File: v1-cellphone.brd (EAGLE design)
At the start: 96 x 45.2 mm, 95 parts, among them J1 AVRISP, J2 ZX62D-B-5P8, J3 GPIO, J4 FTDI, J5 BATTERY INPUT, Q1 MIC, Q2 NTR4501N-D, Q3 NTR4501N-D, U1 MCP73831, U2 MEGA1284, U3 GSM_UC15, U4 TXB0104PWR, X1 SMA, X2 8MHz, X3 CCM03-3002 R102

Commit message: All tracks routed. Needs review and impedance checks.
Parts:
- removed J3: GPIO, SparkFun-Connectors:1X20_LOCK_LONGPADS
- removed TP17, TP2, TP4, TP5: TPPAD1-13, testpad:P1-13
- added JP1, JP2, JP3: (no value), SparkFun-Connectors:1X04_LOCK
- C22, C26: device rcl_custom:0603-B -> rcl_custom:C1210K
- moved SP1 571.4 mm to (96.0, 13.8), turned to 270 degrees
- moved C40 561.8 mm to (31.6, 40.6), turned to 90 degrees
- moved C2 544.5 mm to (39.2, 11.7)
- moved C41 543.2 mm to (44.3, 14.5)
- moved R13 541.2 mm to (45.0, 22.5), turned to 180 degrees
- moved R12 529.3 mm to (95.1, 3.17), turned to 270 degrees
- moved R11 529.2 mm to (97.4, 7.49), turned to 270 degrees
- moved Q3 519.8 mm to (92.3, 3.30), turned to 90 degrees
- moved U4 514.9 mm to (46.4, 18.5), turned to 90 degrees
- moved TP15 489.0 mm to (32.9, 24.0)
- moved TP14 483.4 mm to (34.5, 22.4)
- moved TP12 458.7 mm to (36.2, 24.0)
- moved TP11 453.2 mm to (37.8, 22.4)
- moved R14 451.0 mm to (62.6, 43.8), turned to 180 degrees
- moved TP13 448.1 mm to (4.95, 14.2)
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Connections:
- net N$10 renamed PRESENCE
- net N$14 renamed OE
- net N$16 renamed MIC1P
- net N$19 renamed MIC1N
- net N$7 renamed XTAL2
- net N$8 renamed XTAL1
- net PB4 renamed DEBUGLED
- removed net 2.6V: C39.1, R13.1, TP2.TP, U3.7, U4.1
- new net VDD_EXT: C39.1, R13.1, U3.7, U4.1
- net N$20: no longer TP4.TP
- net N$21: no longer TP5.TP
- net N$23: no longer TP17.TP
- net PA0: now also JP1.1; no longer J3.1
- net PA1: now also JP1.2; no longer J3.2
- net PA2: now also JP1.3; no longer J3.3
- net PA3: now also JP1.4; no longer J3.4
- net PA4: now also JP2.1; no longer J3.5
- net PA5: now also JP2.2; no longer J3.6
- net PA6: now also JP2.3; no longer J3.7
- net PA7: now also JP2.4; no longer J3.8
- net PB0: now also JP3.1; no longer J3.9
- net PB1: now also JP3.2; no longer J3.10
- net PB2: now also JP3.3; no longer J3.11
- net PB3: now also JP3.4; no longer J3.12
- net PC0: no longer J3.13
- net PC1: no longer J3.14
- net PC2: no longer J3.15
- net PC3: no longer J3.16
- net PC4: no longer J3.17
- net PC5: no longer J3.18
- net PC6: no longer J3.19
- net PC7: no longer J3.20
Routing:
- net N$1: track 0.00 -> 84.4 mm, vias 0 -> 2
- net SETUC15RESET: track 0.00 -> 79.5 mm, vias 0 -> 1
- net SETPWRKEY: track 0.00 -> 74.9 mm, vias 0 -> 1
- net SIM_VDD: track 0.00 -> 56.1 mm, vias 0 -> 2
- net SIM_RST: track 0.00 -> 47.1 mm, vias 0 -> 2
- net SIM_CLK: track 0.00 -> 46.7 mm, vias 0 -> 2
- net VDD_EXT: track 0.00 -> 40.6 mm, vias 0 -> 2
- net VBAT: track 0.00 -> 35.2 mm, vias 0 -> 22
- net BATTSTATUS: track 0.00 -> 32.2 mm, vias 0 -> 2
- net AGND: track 0.00 -> 30.5 mm, vias 0 -> 7
- net !RESET: track 0.00 -> 30.1 mm
- net 5V: track 0.00 -> 28.0 mm
- net N$13: track 0.00 -> 27.7 mm
- net MOSI: track 0.00 -> 25.2 mm, vias 0 -> 3
- net SCK: track 0.00 -> 22.9 mm, vias 0 -> 2
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- added copper zone on layer 1, net AGND
- added copper zone on layer 2, net AGND
- added copper zone on layer 1, net GND
- added copper zone on layer 16, net GND
- added copper zone on layer 2, net GND
- added copper zone on layer 1, net MIC1N
- added copper zone on layer 1, net MIC1P
- added copper zone on layer 1, net SPK1N
- added copper zone on layer 1, net SPK1P
- added copper zone on layer 1, net VBAT
- added copper zone on layer 15, net VBAT
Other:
- board size 96 x 45.2 mm -> 103.1 x 46.7 mm
- board text removed: "B"
- board text removed: "G"

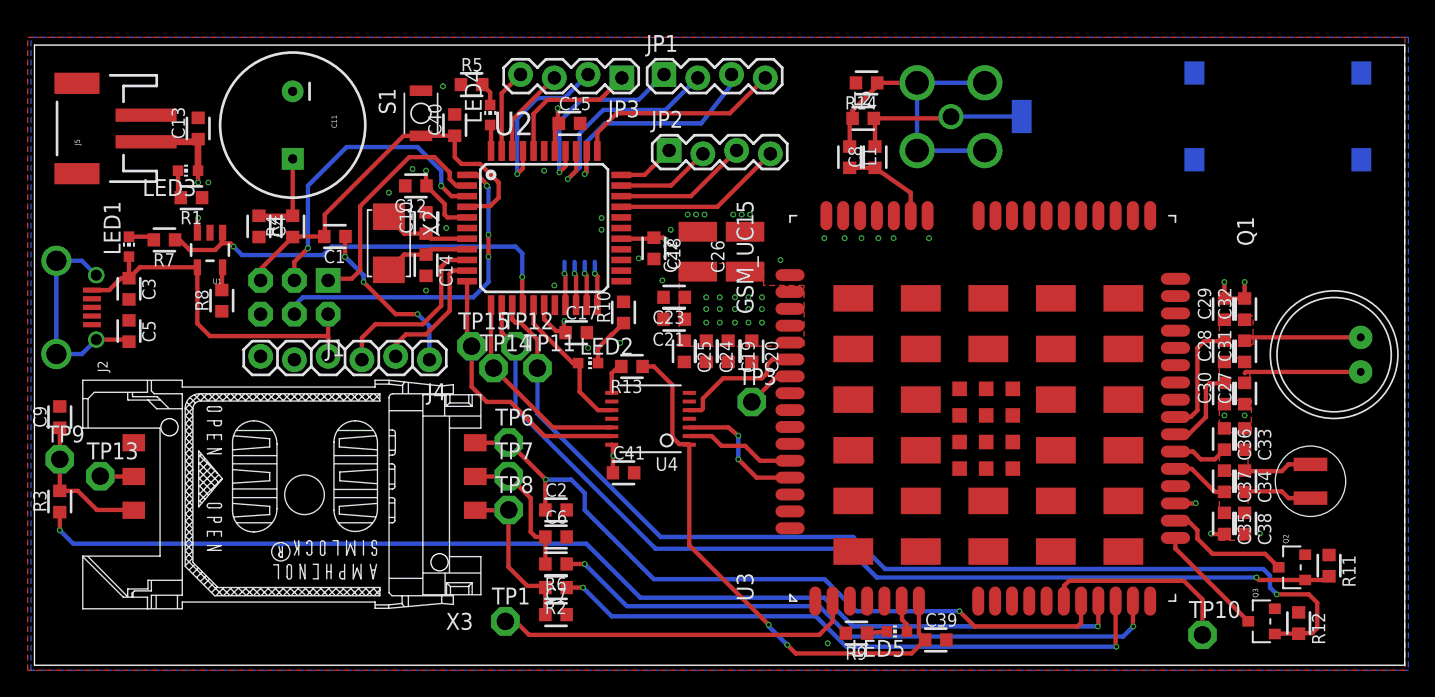
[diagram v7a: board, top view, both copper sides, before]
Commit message: Fixed UC15 package. Passes ERC, DRC. Cleaned silk.
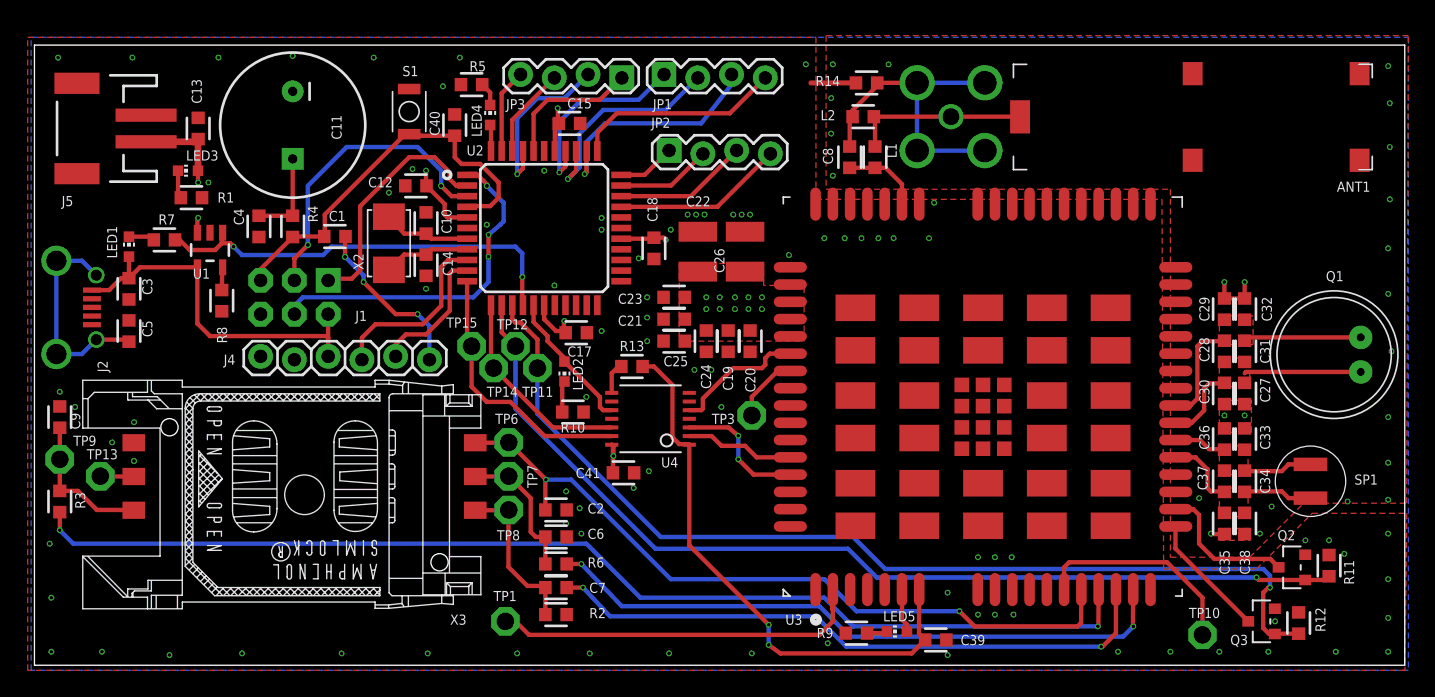
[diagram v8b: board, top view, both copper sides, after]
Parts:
- moved R10 8.41 mm to (40.5, 19.1), turned to 0 degrees
- moved ANT1 7.88 mm to (73.7, 45.2), flipped to the top, turned to 270 degrees
- moved LED2 1.89 mm to (39.9, 22.1), turned to 180 degrees
- moved U3 1.59 mm to (71.4, 20.2)
- moved C25 1.08 mm to (48.1, 24.4), turned to 180 degrees
- moved TP3 1.02 mm to (54.0, 18.8)
- moved S1 0.90 mm to (28.2, 41.7)
- moved C20 0.77 mm to (53.8, 24.4)
- moved C19 0.76 mm to (52.2, 24.4)
- moved C24 0.76 mm to (50.5, 24.4)
- moved L2 0.13 mm to (62.4, 41.3)
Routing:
- net GND: track 0.00 -> 3.39 mm, vias 29 -> 86
- net PC3: track 3.34 -> 0.00 mm, vias 1 -> 0
- net PC2: track 3.32 -> 0.00 mm, vias 1 -> 0
- net PC1: track 3.31 -> 0.00 mm, vias 1 -> 0
- net PC0: track 3.29 -> 0.00 mm, vias 1 -> 0
- net SETUC15RESET: track 79.5 -> 76.4 mm
- net PRESENCE: track 15.0 -> 17.8 mm
- net N$13: track 27.7 -> 29.4 mm
- net NETLIGHT: track 2.47 -> 4.19 mm
- net VDD_EXT: track 40.6 -> 42.2 mm
- net AGND: track 30.5 -> 28.9 mm, vias 7 -> 24
- net N$37: track 3.83 -> 2.37 mm
- net N$15: track 3.67 -> 5.10 mm
- net !PWRKEY: track 9.59 -> 10.8 mm
- net SPK1N: track 9.58 -> 10.7 mm
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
